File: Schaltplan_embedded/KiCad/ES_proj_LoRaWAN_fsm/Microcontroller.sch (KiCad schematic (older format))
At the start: 15 parts, among them J1 Conn_02x05_Odd_Even, SW1 SW_Push, U1 STM32L476RGTx, Y1 Crystal

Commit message: Neuer Schaltplan
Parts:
- C1, C2: footprint (none) -> Capacitors_SMD:C_0603_HandSoldering
- C3, C4, C5, C6, C7: footprint (none) -> Capacitors_SMD:C_0805_HandSoldering
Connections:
- net AntOFF: now reaches U1.61 (PB8)
- net 3V3 renamed +3V3
- no-connect marks 25 -> 24
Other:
- moved on the sheet: C2
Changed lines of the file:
@@
 F 0 "C1" H 1365 4446 50  0000 L CNN
 F 1 "20pF" H 1365 4355 50  0000 L CNN
-F 2 "" H 1288 4250 50  0001 C CNN
+F 2 "Capacitors_SMD:C_0603_HandSoldering" H 1288 4250 50  0001 C CNN
 F 3 "~" H 1250 4400 50  0001 C CNN
 	1    1250 4400
@@
 L Device:C C2
 U 1 1 5DC1A899
-P 2350 4400
-F 0 "C2" H 2465 4446 50  0000 L CNN
-F 1 "20pF" H 2465 4355 50  0000 L CNN
-F 2 "" H 2388 4250 50  0001 C CNN
-F 3 "~" H 2350 4400 50  0001 C CNN
-	1    2350 4400
+P 2300 4400
+F 0 "C2" H 2415 4446 50  0000 L CNN
+F 1 "20pF" H 2415 4355 50  0000 L CNN
+F 2 "Capacitors_SMD:C_0603_HandSoldering" H 2338 4250 50  0001 C CNN
+F 3 "~" H 2300 4400 50  0001 C CNN
+	1    2300 4400
 	1    0    0    -1
 $EndComp
@@
 	1250 4550 1650 4550
 Wire Wire Line
-	2350 4550 1800 4550
+	2300 4550 1800 4550
 Connection ~ 1800 4550
 Wire Wire Line
@@
 	1250 4250 1800 4250
 Wire Wire Line
-	2350 4250 1800 4250
+	2300 4250 1800 4250
 Connection ~ 1800 4250
-Connection ~ 2350 4250
-Connection ~ 2350 4550
-Wire Wire Line
-	2350 4550 3050 4550
-Wire Wire Line
-	2350 4250 3400 4250
+Connection ~ 2300 4250
+Connection ~ 2300 4550
+Wire Wire Line
+	2300 4550 3050 4550
+Wire Wire Line
+	2300 4250 3400 4250
 Wire Wire Line
 	3050 4550 3050 4350
@@
 	1    0    0    -1
 $EndComp
-Text GLabel 4850 1300 0    50   Input ~ 0
-3V3
 $Comp
 L Device:C C3
@@
 F 0 "C3" H 5365 1596 50  0000 L CNN
 F 1 "100n" H 5365 1505 50  0000 L CNN
-F 2 "" H 5288 1400 50  0001 C CNN
+F 2 "Capacitors_SMD:C_0805_HandSoldering" H 5288 1400 50  0001 C CNN
 F 3 "~" H 5250 1550 50  0001 C CNN
 	1    5250 1550
@@
 F 0 "C4" H 5715 1596 50  0000 L CNN
 F 1 "100n" H 5715 1505 50  0000 L CNN
-F 2 "" H 5638 1400 50  0001 C CNN
+F 2 "Capacitors_SMD:C_0805_HandSoldering" H 5638 1400 50  0001 C CNN
 F 3 "~" H 5600 1550 50  0001 C CNN
 	1    5600 1550
@@
 F 0 "C5" H 6065 1596 50  0000 L CNN
 F 1 "100n" H 6065 1505 50  0000 L CNN
-F 2 "" H 5988 1400 50  0001 C CNN
+F 2 "Capacitors_SMD:C_0805_HandSoldering" H 5988 1400 50  0001 C CNN
 F 3 "~" H 5950 1550 50  0001 C CNN
 	1    5950 1550
@@
 F 0 "C6" H 6515 1596 50  0000 L CNN
 F 1 "100n" H 6515 1505 50  0000 L CNN
-F 2 "" H 6438 1400 50  0001 C CNN
+F 2 "Capacitors_SMD:C_0805_HandSoldering" H 6438 1400 50  0001 C CNN
 F 3 "~" H 6400 1550 50  0001 C CNN
 	1    6400 1550
@@
 Wire Wire Line
 	5250 1400 5250 1300
-Connection ~ 5250 1300
 Wire Wire Line
 	5250 1300 5600 1300
@@
 Wire Wire Line
 	6050 1700 5950 1700
-Wire Wire Line
-	4850 1300 5250 1300
-Text GLabel 3850 2650 0    50   Input ~ 0
-3V3
-Wire Wire Line
-	3900 2850 3900 2650
-Wire Wire Line
-	3900 2650 3850 2650
 Connection ~ 5950 1700
 Wire Wire Line
@@
 Text GLabel 6550 4400 0    50   BiDi ~ 0
 JTAG_TMS
-Text GLabel 6550 4500 0    50   BiDi ~ 0
-3V3
 Text GLabel 6550 4600 0    50   BiDi ~ 0
 JTAG_TDI
@@
 L power:GND #PWR0104
 U 1 1 5DC3289B
-P 7250 4600
-F 0 "#PWR0104" H 7250 4350 50  0001 C CNN
-F 1 "GND" H 7255 4427 50  0000 C CNN
-F 2 "" H 7250 4600 50  0001 C CNN
-F 3 "" H 7250 4600 50  0001 C CNN
-	1    7250 4600
+P 7250 4650
+F 0 "#PWR0104" H 7250 4400 50  0001 C CNN
+F 1 "GND" H 7255 4477 50  0000 C CNN
+F 2 "" H 7250 4650 50  0001 C CNN
+F 3 "" H 7250 4650 50  0001 C CNN
+	1    7250 4650
 	1    0    0    -1
 $EndComp
@@
 NoConn ~ 7100 4500
 Wire Wire Line
-	7100 4600 7250 4600
-Wire Wire Line
 	7400 4400 7100 4400
 Wire Wire Line
@@
 Wire Wire Line
 	7250 4200 7250 4600
-Connection ~ 7250 4600
 Wire Wire Line
 	6600 4600 6550 4600
-Wire Wire Line
-	6600 4500 6550 4500
 Wire Wire Line
 	6600 4400 6550 4400
@@
 Text GLabel 8650 2800 2    50   Output ~ 0
 JTAG_RESET
-Text GLabel 8550 2150 2    50   Input ~ 0
-3V3
 $Comp
 L power:GND #PWR0105
@@
 F 0 "C7" H 8515 2996 50  0000 L CNN
 F 1 "100nF" H 8515 2905 50  0000 L CNN
-F 2 "" H 8438 2800 50  0001 C CNN
+F 2 "Capacitors_SMD:C_0805_HandSoldering" H 8438 2800 50  0001 C CNN
 F 3 "~" H 8400 2950 50  0001 C CNN
 	1    8400 2950
@@
 	1    0    0    -1
 $EndComp
-Wire Wire Line
-	8550 2150 8400 2150
-Wire Wire Line
-	8400 2150 8400 2400
 Wire Wire Line
 	8400 2800 8400 2700
@@
 Text GLabel 5100 4050 2    51   Output ~ 0
 5V_ENABLE
-Wire Wire Line
-	5100 4050 4800 4050
-NoConn ~ 4800 5550
 NoConn ~ 4800 5450
 NoConn ~ 4800 5350
@@
 Text GLabel 5100 3850 2    50   Output ~ 0
 GPS_WAKEUP
-Wire Wire Line
-	4800 3850 5100 3850
 Text GLabel 5100 3350 2    50   Output ~ 0
 GPS_RSTN
@@
 Wire Wire Line
 	4800 5650 5100 5650
-Wire Wire Line
-	4300 2850 4400 2850
-Connection ~ 4300 2850
-Wire Wire Line
-	4200 2850 4300 2850
-Connection ~ 4200 2850
-Wire Wire Line
-	4100 2850 4200 2850
-Connection ~ 4100 2850
-Wire Wire Line
-	3900 2850 4000 2850
-Wire Wire Line
-	4100 2850 4000 2850
-Connection ~ 4000 2850
-Connection ~ 3900 2850
 $Comp
 L MCU_ST_STM32L4:STM32L476RGTx U1
@@
 Wire Wire Line
 	4100 6550 4100 6650
+Wire Wire Line
+	3900 2750 4000 2750
+Wire Wire Line
+	4000 2750 4000 2850
+Connection ~ 3900 2750
+Wire Wire Line
+	3900 2750 3900 2850
+Wire Wire Line
+	4000 2750 4100 2750
+Wire Wire Line
+	4100 2750 4100 2850
+Connection ~ 4000 2750
+Wire Wire Line
+	4100 2750 4200 2750
+Wire Wire Line
+	4200 2750 4200 2850
+Connection ~ 4100 2750
+Wire Wire Line
+	4200 2750 4300 2750
+Wire Wire Line
+	4300 2750 4300 2850
+Connection ~ 4200 2750
+Wire Wire Line
+	4300 2750 4400 2750
+Wire Wire Line
+	4400 2750 4400 2850
+Connection ~ 4300 2750
+Text GLabel 5100 5550 2    50   Output ~ 0
+AntOFF
+Wire Wire Line
+	4800 5550 5100 5550
+Wire Wire Line
+	4800 4050 5100 4050
+Wire Wire Line
+	4800 3850 5100 3850
+$Comp
+L power:+3.3V #PWR0114
+U 1 1 5DEBFF94
+P 3900 2600
+F 0 "#PWR0114" H 3900 2450 50  0001 C CNN
+F 1 "+3.3V" H 3915 2773 50  0000 C CNN
+F 2 "" H 3900 2600 50  0001 C CNN
+F 3 "" H 3900 2600 50  0001 C CNN
+	1    3900 2600
+	1    0    0    -1
+$EndComp
+$Comp
+L power:+3.3V #PWR0115
+U 1 1 5DEC0739
+P 8400 2050
+F 0 "#PWR0115" H 8400 1900 50  0001 C CNN
+F 1 "+3.3V" H 8415 2223 50  0000 C CNN
+F 2 "" H 8400 2050 50  0001 C CNN
+F 3 "" H 8400 2050 50  0001 C CNN
+	1    8400 2050
+	1    0    0    -1
+$EndComp
+$Comp
+L power:+3.3V #PWR0116
+U 1 1 5DEC0C78
+P 5250 1100
+F 0 "#PWR0116" H 5250 950 50  0001 C CNN
+F 1 "+3.3V" H 5265 1273 50  0000 C CNN
+F 2 "" H 5250 1100 50  0001 C CNN
+F 3 "" H 5250 1100 50  0001 C CNN
+	1    5250 1100
+	1    0    0    -1
+$EndComp
+$Comp
+L power:+3.3V #PWR0117
+U 1 1 5DEC1290
+P 5950 4050
+F 0 "#PWR0117" H 5950 3900 50  0001 C CNN
+F 1 "+3.3V" H 5965 4223 50  0000 C CNN
+F 2 "" H 5950 4050 50  0001 C CNN
+F 3 "" H 5950 4050 50  0001 C CNN
+	1    5950 4050
+	1    0    0    -1
+$EndComp
+Wire Wire Line
+	3900 2600 3900 2750
+Wire Wire Line
+	6600 4500 5950 4500
+Wire Wire Line
+	5950 4500 5950 4050
+Wire Wire Line
+	8400 2050 8400 2400
+Wire Wire Line
+	5250 1100 5250 1300
+Connection ~ 5250 1300
+Wire Wire Line
+	7100 4600 7250 4600
+Connection ~ 7250 4600
+Wire Wire Line
+	7250 4600 7250 4650
 $EndSCHEMATC

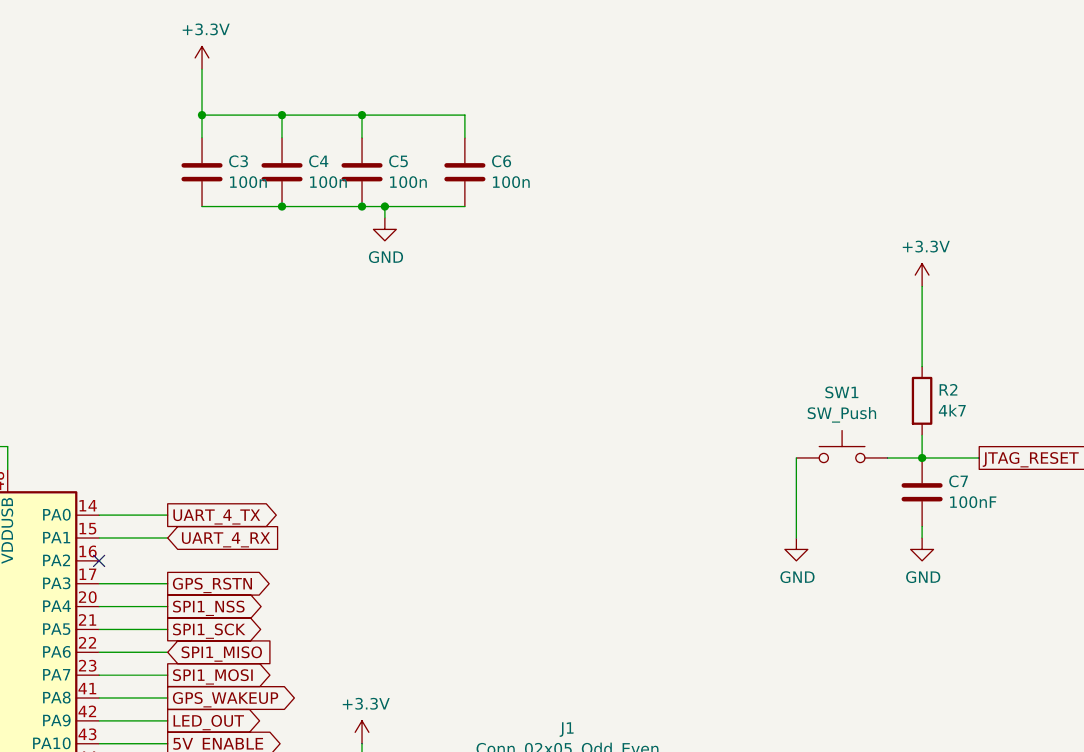
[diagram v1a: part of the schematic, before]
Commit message: Bauteilliste vollständig und Schaltplan entsprechend geändert
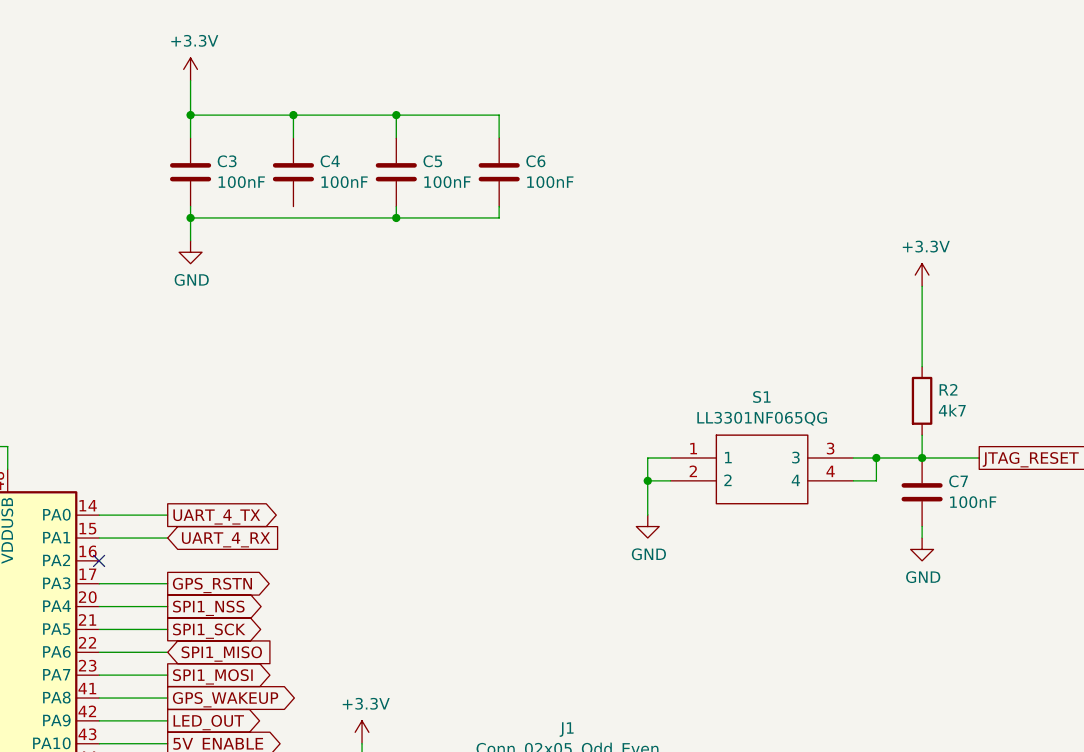
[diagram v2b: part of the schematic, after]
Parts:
- removed SW1: SW_Push, symbol Switch:SW_Push
- added S1: LL3301NF065QG, SamacSys_Parts:LL3301NF065QG, symbol SamacSys_Parts:LL3301NF065QG
- C3, C4, C5, C6: value 100n -> 100nF
- D1: footprint (none) -> LEDs:LED_0805_HandSoldering
- J1: footprint (none) -> Connectors_JAE:JAE_LY20-10P-2T_2x05x2.00mm_Straight
- R1, R2, R3: footprint (none) -> Resistors_SMD:R_0805_HandSoldering
- U1: footprint Package_QFP:LQFP-64_10x10mm_P0.5mm -> Housings_QFP:LQFP-64_10x10mm_Pitch0.5mm
- Y1: footprint (none) -> SamacSys_Parts:ABS2532768KHZT
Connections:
- net GND: now also S1.1, S1.2; no longer C4.2
- net JTAG_RESET: now also S1.3, S1.4
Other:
- moved on the sheet: C3, C4, C5, C6
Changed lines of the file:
@@
 F 0 "Y1" V 1754 4531 50  0000 L CNN
 F 1 "Crystal" V 1845 4531 50  0000 L CNN
-F 2 "" H 1800 4400 50  0001 C CNN
+F 2 "SamacSys_Parts:ABS2532768KHZT" H 1800 4400 50  0001 C CNN
 F 3 "~" H 1800 4400 50  0001 C CNN
 	1    1800 4400
@@
 L Device:C C3
 U 1 1 5DC1C228
-P 5250 1550
-F 0 "C3" H 5365 1596 50  0000 L CNN
-F 1 "100n" H 5365 1505 50  0000 L CNN
-F 2 "Capacitors_SMD:C_0805_HandSoldering" H 5288 1400 50  0001 C CNN
-F 3 "~" H 5250 1550 50  0001 C CNN
-	1    5250 1550
+P 5200 1550
+F 0 "C3" H 5315 1596 50  0000 L CNN
+F 1 "100nF" H 5315 1505 50  0000 L CNN
+F 2 "Capacitors_SMD:C_0805_HandSoldering" H 5238 1400 50  0001 C CNN
+F 3 "~" H 5200 1550 50  0001 C CNN
+	1    5200 1550
 	1    0    0    -1
 $EndComp
@@
 L Device:C C4
 U 1 1 5DC1C2AE
-P 5600 1550
-F 0 "C4" H 5715 1596 50  0000 L CNN
-F 1 "100n" H 5715 1505 50  0000 L CNN
-F 2 "Capacitors_SMD:C_0805_HandSoldering" H 5638 1400 50  0001 C CNN
-F 3 "~" H 5600 1550 50  0001 C CNN
-	1    5600 1550
+P 5650 1550
+F 0 "C4" H 5765 1596 50  0000 L CNN
+F 1 "100nF" H 5765 1505 50  0000 L CNN
+F 2 "Capacitors_SMD:C_0805_HandSoldering" H 5688 1400 50  0001 C CNN
+F 3 "~" H 5650 1550 50  0001 C CNN
+	1    5650 1550
 	1    0    0    -1
 $EndComp
@@
 L Device:C C5
 U 1 1 5DC1C579
-P 5950 1550
-F 0 "C5" H 6065 1596 50  0000 L CNN
-F 1 "100n" H 6065 1505 50  0000 L CNN
-F 2 "Capacitors_SMD:C_0805_HandSoldering" H 5988 1400 50  0001 C CNN
-F 3 "~" H 5950 1550 50  0001 C CNN
-	1    5950 1550
+P 6100 1550
+F 0 "C5" H 6215 1596 50  0000 L CNN
+F 1 "100nF" H 6215 1505 50  0000 L CNN
+F 2 "Capacitors_SMD:C_0805_HandSoldering" H 6138 1400 50  0001 C CNN
+F 3 "~" H 6100 1550 50  0001 C CNN
+	1    6100 1550
 	1    0    0    -1
 $EndComp
@@
 L Device:C C6
 U 1 1 5DC1C7FD
-P 6400 1550
-F 0 "C6" H 6515 1596 50  0000 L CNN
-F 1 "100n" H 6515 1505 50  0000 L CNN
-F 2 "Capacitors_SMD:C_0805_HandSoldering" H 6438 1400 50  0001 C CNN
-F 3 "~" H 6400 1550 50  0001 C CNN
-	1    6400 1550
-	1    0    0    -1
-$EndComp
-Wire Wire Line
-	5250 1400 5250 1300
-Wire Wire Line
-	5250 1300 5600 1300
-Wire Wire Line
-	5600 1400 5600 1300
-Connection ~ 5600 1300
-Wire Wire Line
-	5600 1300 5950 1300
-Wire Wire Line
-	5950 1400 5950 1300
-Connection ~ 5950 1300
-Wire Wire Line
-	6400 1700 6050 1700
+P 6550 1550
+F 0 "C6" H 6665 1596 50  0000 L CNN
+F 1 "100nF" H 6665 1505 50  0000 L CNN
+F 2 "Capacitors_SMD:C_0805_HandSoldering" H 6588 1400 50  0001 C CNN
+F 3 "~" H 6550 1550 50  0001 C CNN
+	1    6550 1550
+	1    0    0    -1
+$EndComp
+Wire Wire Line
+	5200 1400 5200 1300
+Wire Wire Line
+	5200 1300 5650 1300
+Wire Wire Line
+	5650 1400 5650 1300
+Connection ~ 5650 1300
+Wire Wire Line
+	5650 1300 6100 1300
+Wire Wire Line
+	6100 1400 6100 1300
+Connection ~ 6100 1300
 $Comp
 L power:GND #PWR0103
 U 1 1 5DC1EF80
-P 6050 1750
-F 0 "#PWR0103" H 6050 1500 50  0001 C CNN
-F 1 "GND" H 6055 1577 50  0000 C CNN
-F 2 "" H 6050 1750 50  0001 C CNN
-F 3 "" H 6050 1750 50  0001 C CNN
-	1    6050 1750
-	1    0    0    -1
-$EndComp
-Wire Wire Line
-	6050 1750 6050 1700
-Connection ~ 6050 1700
-Wire Wire Line
-	6050 1700 5950 1700
-Connection ~ 5950 1700
-Wire Wire Line
-	5600 1700 5950 1700
-Connection ~ 5600 1700
-Wire Wire Line
-	5250 1700 5600 1700
-Wire Wire Line
-	5950 1300 6400 1300
-Wire Wire Line
-	6400 1300 6400 1400
+P 5200 1850
+F 0 "#PWR0103" H 5200 1600 50  0001 C CNN
+F 1 "GND" H 5205 1677 50  0000 C CNN
+F 2 "" H 5200 1850 50  0001 C CNN
+F 3 "" H 5200 1850 50  0001 C CNN
+	1    5200 1850
+	1    0    0    -1
+$EndComp
+Wire Wire Line
+	6100 1300 6550 1300
+Wire Wire Line
+	6550 1300 6550 1400
 Text GLabel 5100 3450 2    50   Output ~ 0
 SPI1_NSS
@@
 F 0 "J1" H 6850 4817 50  0000 C CNN
 F 1 "Conn_02x05_Odd_Even" H 6850 4726 50  0000 C CNN
-F 2 "" H 6800 4400 50  0001 C CNN
+F 2 "Connectors_JAE:JAE_LY20-10P-2T_2x05x2.00mm_Straight" H 6800 4400 50  0001 C CNN
 F 3 "~" H 6800 4400 50  0001 C CNN
 	1    6800 4400
@@
 	1    0    0    -1
 $EndComp
-$Comp
-L power:GND #PWR0106
-U 1 1 5DC3DC91
-P 7850 3150
-F 0 "#PWR0106" H 7850 2900 50  0001 C CNN
-F 1 "GND" H 7855 2977 50  0000 C CNN
-F 2 "" H 7850 3150 50  0001 C CNN
-F 3 "" H 7850 3150 50  0001 C CNN
-	1    7850 3150
-	1    0    0    -1
-$EndComp
-$Comp
-L Switch:SW_Push SW1
-U 1 1 5DC3DD7D
-P 8050 2800
-F 0 "SW1" H 8050 3085 50  0000 C CNN
-F 1 "SW_Push" H 8050 2994 50  0000 C CNN
-F 2 "" H 8050 3000 50  0001 C CNN
-F 3 "" H 8050 3000 50  0001 C CNN
-	1    8050 2800
-	1    0    0    -1
-$EndComp
-Wire Wire Line
-	7850 2800 7850 3150
-Wire Wire Line
-	8250 2800 8400 2800
 Wire Wire Line
 	8650 2800 8400 2800
@@
 F 0 "R2" H 8470 2596 50  0000 L CNN
 F 1 "4k7" H 8470 2505 50  0000 L CNN
-F 2 "" V 8330 2550 50  0001 C CNN
+F 2 "Resistors_SMD:R_0805_HandSoldering" V 8330 2550 50  0001 C CNN
 F 3 "~" H 8400 2550 50  0001 C CNN
 	1    8400 2550
@@
 F 0 "R1" V 3150 3250 50  0000 C CNN
 F 1 "100k" V 3250 3250 50  0000 C CNN
-F 2 "" V 2980 3250 50  0001 C CNN
+F 2 "Resistors_SMD:R_0805_HandSoldering" V 2980 3250 50  0001 C CNN
 F 3 "~" H 3050 3250 50  0001 C CNN
 	1    3050 3250
@@
 F 0 "R3" V 8843 4350 50  0000 C CNN
 F 1 "510" V 8934 4350 50  0000 C CNN
-F 2 "" V 8980 4350 50  0001 C CNN
+F 2 "Resistors_SMD:R_0805_HandSoldering" V 8980 4350 50  0001 C CNN
 F 3 "~" H 9050 4350 50  0001 C CNN
 	1    9050 4350
@@
 F 0 "D1" H 9392 4095 50  0000 C CNN
 F 1 "LED" H 9392 4186 50  0000 C CNN
-F 2 "" H 9400 4350 50  0001 C CNN
+F 2 "LEDs:LED_0805_HandSoldering" H 9400 4350 50  0001 C CNN
 F 3 "~" H 9400 4350 50  0001 C CNN
 	1    9400 4350
@@
 F 0 "U1" H 4400 2900 50  0000 C CNN
 F 1 "STM32L476RGTx" H 4650 2800 50  0000 C CNN
-F 2 "Package_QFP:LQFP-64_10x10mm_P0.5mm" H 3500 2950 50  0001 R CNN
+F 2 "Housings_QFP:LQFP-64_10x10mm_Pitch0.5mm" H 3500 2950 50  0001 R CNN
 F 3 "http://www.st.com/st-web-ui/static/active/en/resource/technical/document/datasheet/DM00108832.pdf" H 4100 4650 50  0001 C CNN
 	1    4100 4650
@@
 L power:+3.3V #PWR0116
 U 1 1 5DEC0C78
-P 5250 1100
-F 0 "#PWR0116" H 5250 950 50  0001 C CNN
-F 1 "+3.3V" H 5265 1273 50  0000 C CNN
-F 2 "" H 5250 1100 50  0001 C CNN
-F 3 "" H 5250 1100 50  0001 C CNN
-	1    5250 1100
+P 5200 1150
+F 0 "#PWR0116" H 5200 1000 50  0001 C CNN
+F 1 "+3.3V" H 5215 1323 50  0000 C CNN
+F 2 "" H 5200 1150 50  0001 C CNN
+F 3 "" H 5200 1150 50  0001 C CNN
+	1    5200 1150
 	1    0    0    -1
 $EndComp
@@
 	8400 2050 8400 2400
 Wire Wire Line
-	5250 1100 5250 1300
-Connection ~ 5250 1300
+	5200 1150 5200 1300
+Connection ~ 5200 1300
 Wire Wire Line
 	7100 4600 7250 4600
@@
 Wire Wire Line
 	7250 4600 7250 4650
+Wire Wire Line
+	5200 1700 5200 1750
+Wire Wire Line
+	6550 1750 6550 1700
+Connection ~ 5200 1750
+Wire Wire Line
+	5200 1750 5200 1850
+Wire Wire Line
+	6100 1700 6100 1750
+Connection ~ 6100 1750
+Wire Wire Line
+	6100 1750 6550 1750
+$Comp
+L power:GND #PWR0106
+U 1 1 5DC3DC91
+P 7200 3050
+F 0 "#PWR0106" H 7200 2800 50  0001 C CNN
+F 1 "GND" H 7205 2877 50  0000 C CNN
+F 2 "" H 7200 3050 50  0001 C CNN
+F 3 "" H 7200 3050 50  0001 C CNN
+	1    7200 3050
+	1    0    0    -1
+$EndComp
+Wire Wire Line
+	5200 1750 6100 1750
+Wire Wire Line
+	8100 2800 8200 2800
+$Comp
+L SamacSys_Parts:LL3301NF065QG S1
+U 1 1 5DE990BE
+P 7300 2800
+F 0 "S1" H 7700 3065 50  0000 C CNN
+F 1 "LL3301NF065QG" H 7700 2974 50  0000 C CNN
+F 2 "SamacSys_Parts:LL3301NF065QG" H 7950 2900 50  0001 L CNN
+F 3 "https://componentsearchengine.com/Datasheets/1/LL3301NF065QG.pdf" H 7950 2800 50  0001 L CNN
+F 4 "E-SWITCH - LL3301NF065QG - TACTILE SW, SPST, 0.05A, 12VDC, SOLDER" H 7950 2700 50  0001 L CNN "Description"
+F 5 "4" H 7950 2600 50  0001 L CNN "Height"
+F 6 "612-LL3301NF065QG" H 7950 2500 50  0001 L CNN "Mouser Part Number"
+F 7 "https://www.mouser.com/Search/Refine.aspx?Keyword=612-LL3301NF065QG" H 7950 2400 50  0001 L CNN "Mouser Price/Stock"
+F 8 "E-Switch" H 7950 2300 50  0001 L CNN "Manufacturer_Name"
+F 9 "LL3301NF065QG" H 7950 2200 50  0001 L CNN "Manufacturer_Part_Number"
+	1    7300 2800
+	1    0    0    -1
+$EndComp
+Wire Wire Line
+	7300 2800 7200 2800
+Wire Wire Line
+	7200 2800 7200 2900
+Wire Wire Line
+	7200 2900 7300 2900
+Connection ~ 7200 2900
+Wire Wire Line
+	7200 2900 7200 3050
+Wire Wire Line
+	8100 2900 8200 2900
+Wire Wire Line
+	8200 2900 8200 2800
+Connection ~ 8200 2800
+Wire Wire Line
+	8200 2800 8400 2800
 $EndSCHEMATC
